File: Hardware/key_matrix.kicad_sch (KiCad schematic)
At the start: 192 parts, among them SW1 F7, SW10 8, SW11 9, SW12 0, SW13 -/_, SW14 +/=, SW15 BS, SW16 PAGE_DOWN, SW17 Y, SW18 U, SW19 I, SW2 F8, SW20 O, SW21 P, SW22 [, SW23 ], SW24 \, SW25 H, SW26 B, SW27 Space, SW28 J, SW29 N, SW3 F9, SW30 R_ALT, SW31 K, SW32 M, SW33 R_WIN, SW34 L, SW35 ,, SW36 R_FCT, SW37 ;, SW38 ., SW39 R_CTRL, SW4 F10, SW40 ', SW41 /, SW42 ARROW_L, SW43 RET, SW44 R_SHIFT, SW45 ARROW_D, SW46 HOME, SW47 ARROW_U, SW48 ARROW_R, SW49 ?, SW5 F11, SW50 ?, SW51 ?, SW52 ?, SW53 ?, SW54 ?, SW55 ESC, SW57 ?, SW58 ?, SW59 ?, SW6 F12, SW60 ?, SW61 F1, SW62 1, SW63 TAB, SW64 CAPS, SW65 L_SHIFT, SW66 ?, SW67 F2, SW68 2, SW69 Q, SW7 DEL, SW70 A, SW71 Z, SW72 ?, SW73 F3, SW74 3, SW75 W, SW76 S, SW77 X, SW78 L_CTRL, SW79 F4, SW8 PAGE_UP, SW80 4, SW81 E, SW82 D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

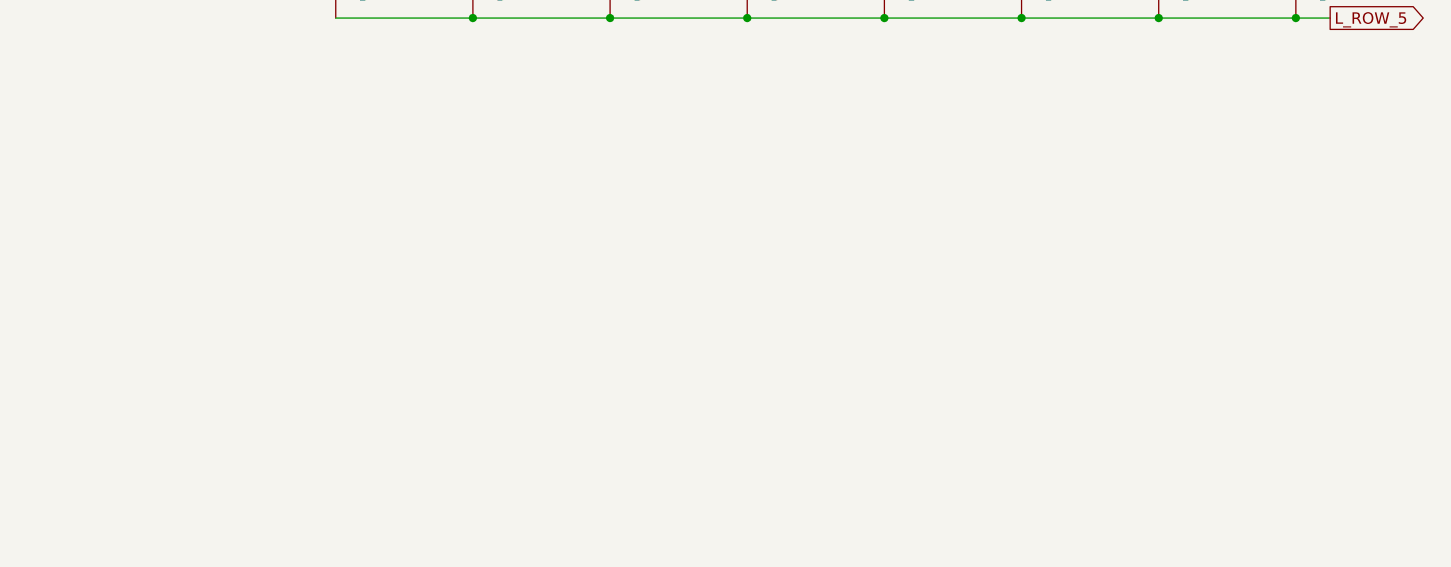
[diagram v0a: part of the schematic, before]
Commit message: Add design notes to key_matrix schematic
Inserted a text block in key_matrix.kicad_sch detailing desired key layout and requirements for the left hand side of the keyboard.
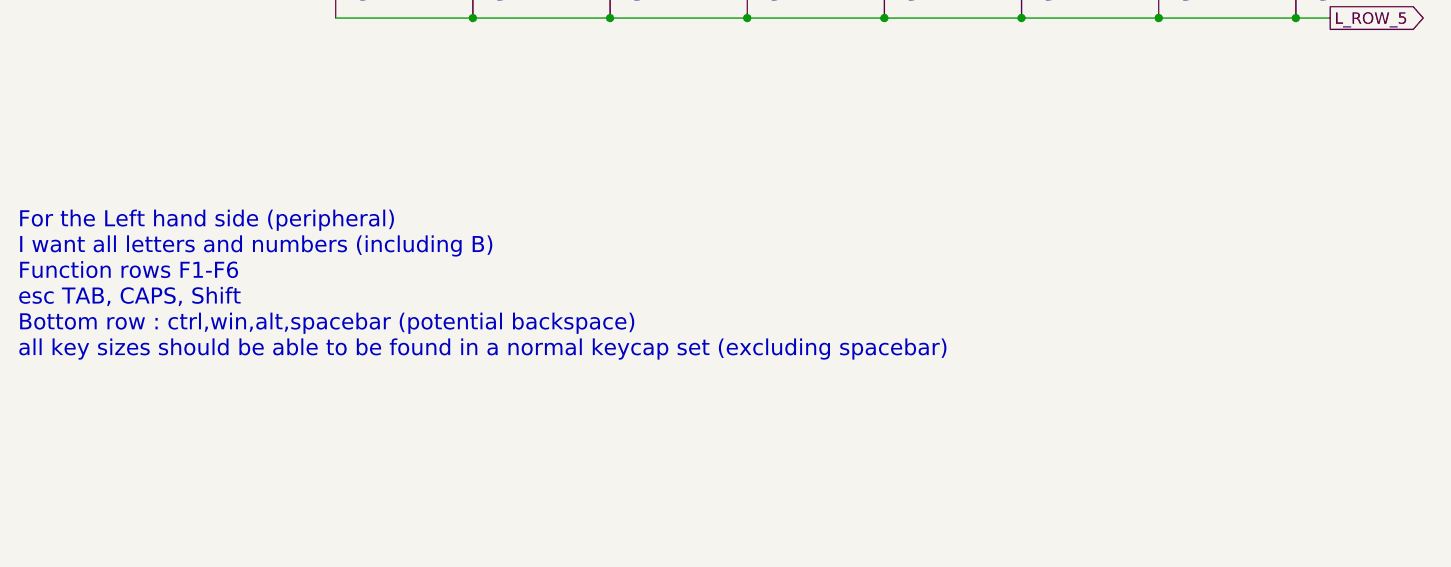
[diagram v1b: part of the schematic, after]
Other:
- note added: "For the Left hand side (peripheral) I want all letters and numbers (including B) Function rows F1-F6 esc TAB, CAPS, Shift Bottom row : ctrl,win,alt,spacebar (potential backspace) all key sizes should be able to be found in a normal keycap set (excluding spacebar)"
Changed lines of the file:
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@@
+		)
+	)
+	(text "For the Left hand side (peripheral)\nI want all letters and numbers (including B)\nFunction rows F1-F6\nesc TAB, CAPS, Shift\nBottom row : ctrl,win,alt,spacebar (potential backspace)\nall key sizes should be able to be found in a normal keycap set (excluding spacebar)"
+		(exclude_from_sim no)
+		(at 19.304 202.438 0)
+		(effects
+			(font
+				(size 1.778 1.778)
+			)
+			(justify left)
 		)
 	)

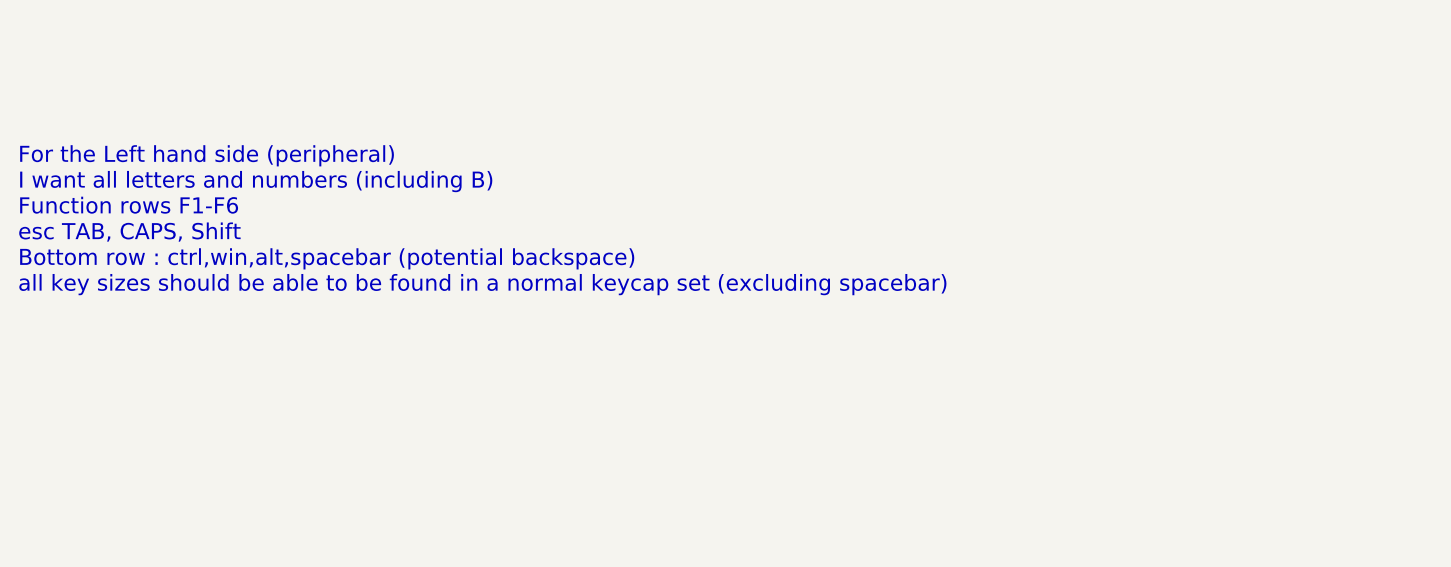
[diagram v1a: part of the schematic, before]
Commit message: finish draft of power schematic
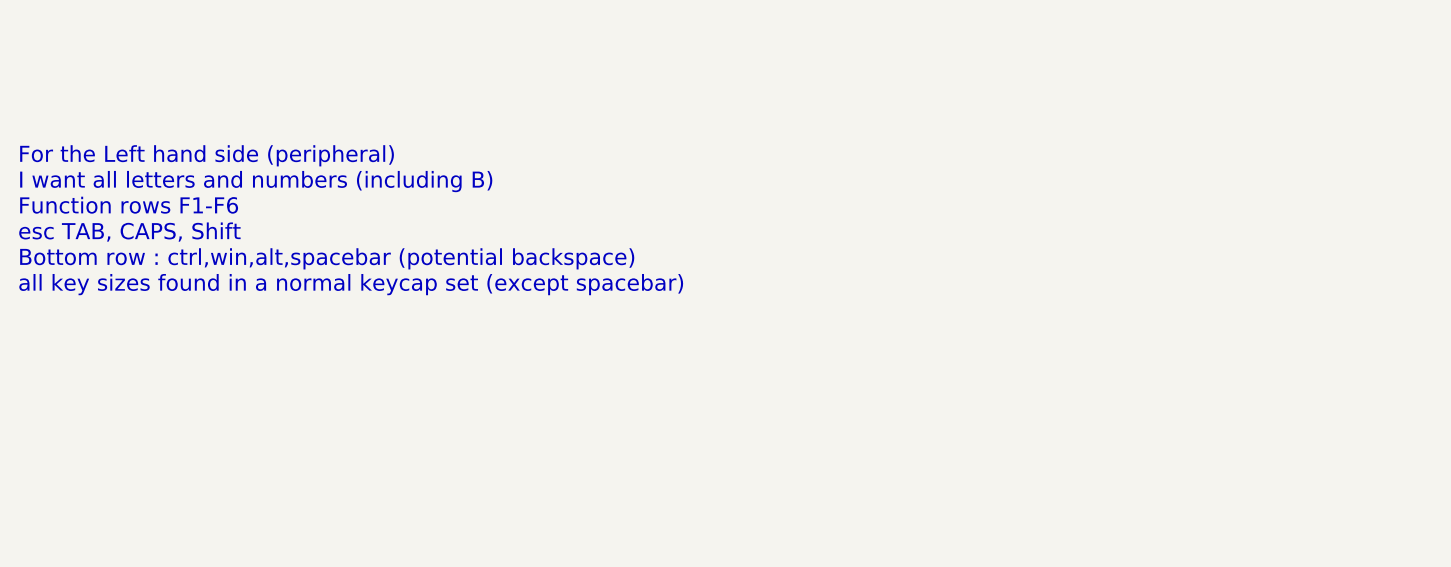
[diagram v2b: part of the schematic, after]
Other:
- note added: "For the Left hand side (peripheral) I want all letters and numbers (including B) Function rows F1-F6 esc TAB, CAPS, Shift Bottom row : ctrl,win,alt,spacebar (potential backspace) all key sizes found in a normal keycap set (except spacebar)"
- note removed: "For the Left hand side (peripheral) I want all letters and numbers (including B) Function rows F1-F6 esc TAB, CAPS, Shift Bottom row : ctrl,win,alt,spacebar (potential backspace) all key sizes should be able to be found in a normal keycap set (excluding spacebar)"

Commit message: Complete first ROUGH draft of schematic
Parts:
- removed D49, D50, D51, D52, D53, D54, D55, D56, D57, D58, D59, D60, D61, D62, D63, D64, D65, D66, D67, D68, D69, D70, D71, D72, D73, D74, D75, D76, D77, D78, D79, D80, D81, D82, D83, D84, D85, D86, D87, D88, D89, D90, D91, D92, D93, D94, D95, D96: D, ScottoKeebs_Components:Diode_SOD-123, symbol Device:D
- removed SW49, SW50, SW51, SW52, SW53, SW54, SW57, SW58, SW59, SW60, SW66, SW72: ?, symbol Switch:SW_Push_45deg
- removed SW55: ESC, symbol Switch:SW_Push_45deg
- removed SW56: ~, symbol Switch:SW_Push_45deg
- removed SW61: F1, symbol Switch:SW_Push_45deg
- removed SW62: 1, symbol Switch:SW_Push_45deg
- removed SW63: TAB, symbol Switch:SW_Push_45deg
- removed SW64: CAPS, symbol Switch:SW_Push_45deg
- removed SW65: L_SHIFT, symbol Switch:SW_Push_45deg
- removed SW67: F2, symbol Switch:SW_Push_45deg
- removed SW68: 2, symbol Switch:SW_Push_45deg
- removed SW69: Q, symbol Switch:SW_Push_45deg
- removed SW70: A, symbol Switch:SW_Push_45deg
- removed SW71: Z, symbol Switch:SW_Push_45deg
- removed SW73: F3, symbol Switch:SW_Push_45deg
- removed SW74: 3, symbol Switch:SW_Push_45deg
- removed SW75: W, symbol Switch:SW_Push_45deg
- removed SW76: S, symbol Switch:SW_Push_45deg
- removed SW77: X, symbol Switch:SW_Push_45deg
- removed SW78: L_CTRL, symbol Switch:SW_Push_45deg
- removed SW79: F4, symbol Switch:SW_Push_45deg
- removed SW80: 4, symbol Switch:SW_Push_45deg
- removed SW81: E, symbol Switch:SW_Push_45deg
- removed SW82: D, symbol Switch:SW_Push_45deg
- removed SW83: C, symbol Switch:SW_Push_45deg
- removed SW84: L_WIN, symbol Switch:SW_Push_45deg
- removed SW85: F5, symbol Switch:SW_Push_45deg
- removed SW86: 5, symbol Switch:SW_Push_45deg
- removed SW87: R, symbol Switch:SW_Push_45deg
- removed SW88: F, symbol Switch:SW_Push_45deg
- removed SW89: V, symbol Switch:SW_Push_45deg
- removed SW90: L_ALT, symbol Switch:SW_Push_45deg
- removed SW91: F6, symbol Switch:SW_Push_45deg
- removed SW92: 6, symbol Switch:SW_Push_45deg
- removed SW93: T, symbol Switch:SW_Push_45deg
- removed SW94: G, symbol Switch:SW_Push_45deg
- removed SW95: B, symbol Switch:SW_Push_45deg
- removed SW96: L_SPACE, symbol Switch:SW_Push_45deg
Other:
- note removed: "LHS"
- moved on the sheet: D1, D10, D11, D12, D13, D14, D15, D16, D17, D18, D19, D2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

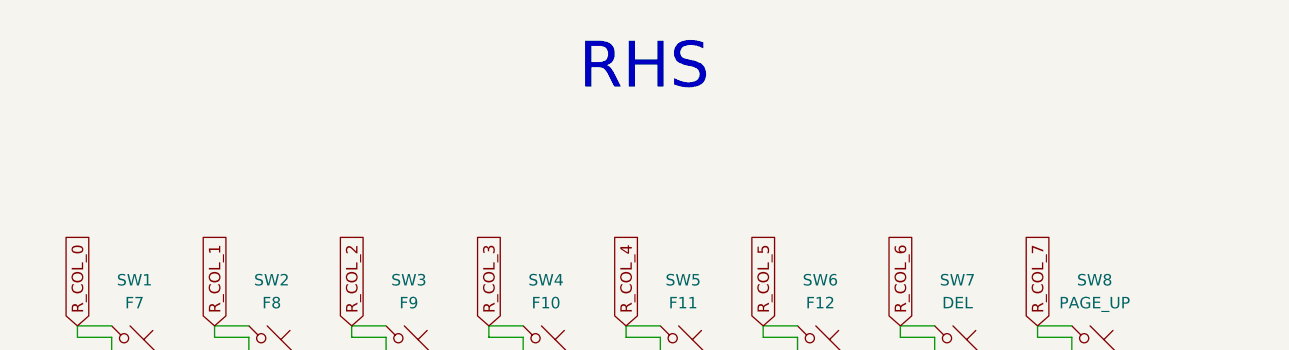
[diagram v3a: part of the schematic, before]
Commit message: renamed layout to left hand central
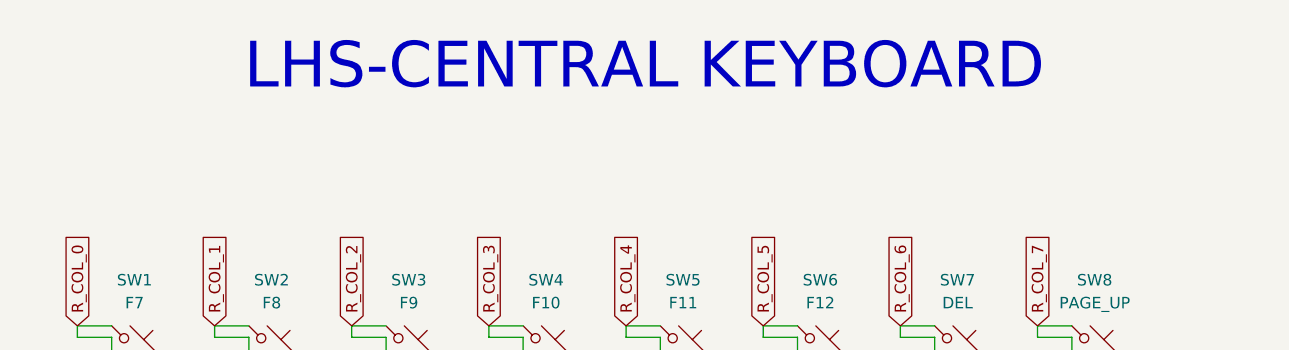
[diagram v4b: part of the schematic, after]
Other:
- note added: "LHS-CENTRAL KEYBOARD"
- note removed: "RHS"
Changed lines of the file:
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@@
 		)
 	)
-	(text "RHS\n"
+	(text "LHS-CENTRAL KEYBOARD"
 		(exclude_from_sim no)
 		(at 207.772 25.908 0)
